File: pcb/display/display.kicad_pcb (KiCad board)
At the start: 2 copper layers, 15 x 44.2 mm, 7 parts, among them J1 INPUT, J2 OUTPUT, J3 UP, J4 DOWN, U1 74HC595

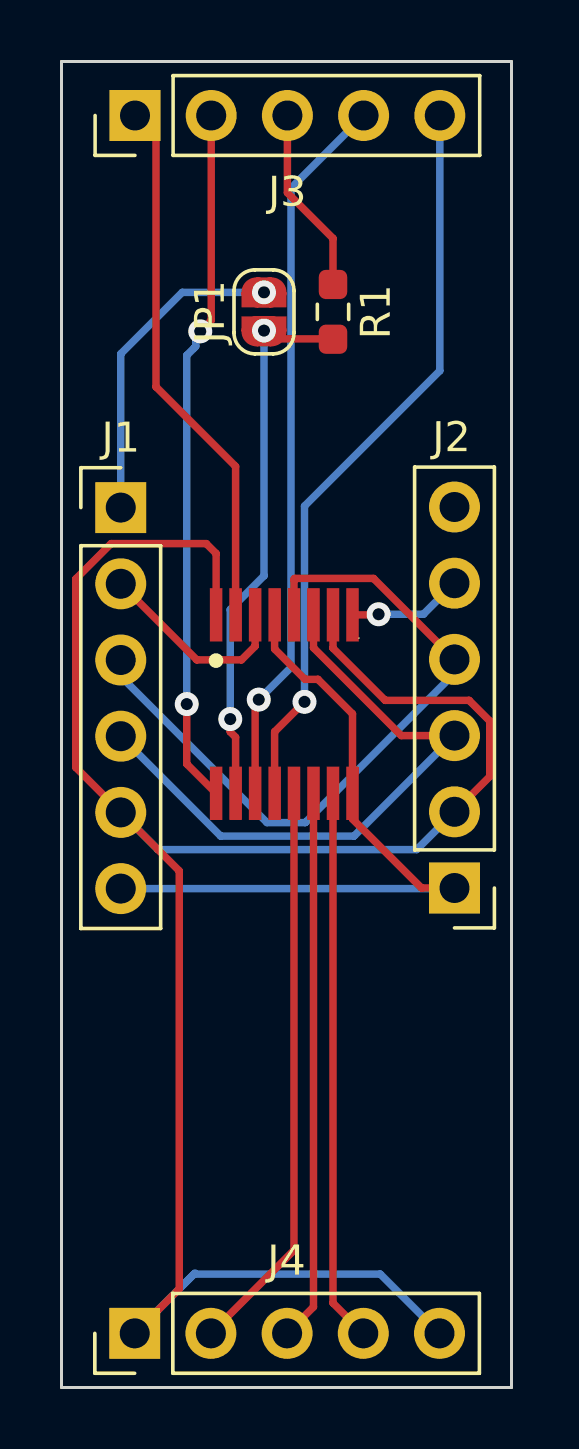
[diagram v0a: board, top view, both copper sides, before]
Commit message: chore: better silkscreen naming on display pcb
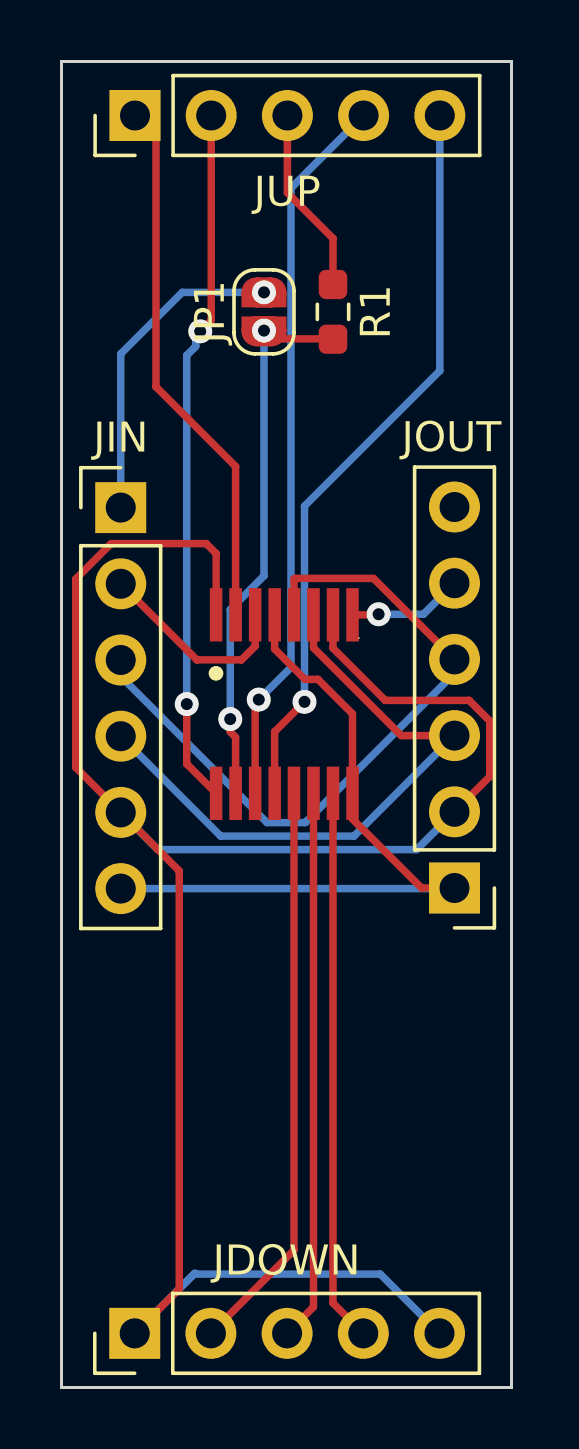
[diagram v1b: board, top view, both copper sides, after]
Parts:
- renumbered J4 to JDOWN, J1 to JIN, J2 to JOUT, J3 to JUP
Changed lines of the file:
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@@
 		(descr "Through hole straight pin header, 1x06, 2.54mm pitch, single row")
 		(tags "Through hole pin header THT 1x06 2.54mm single row")
-		(property "Reference" "J2"
+		(property "Reference" "JOUT"
 			(at 0.1 15.025 180)
 			(layer "F.SilkS")
@@
 		(descr "Through hole straight pin header, 1x05, 2.54mm pitch, single row")
 		(tags "Through hole pin header THT 1x05 2.54mm single row")
-		(property "Reference" "J4"
+		(property "Reference" "JDOWN"
 			(at 2.425 5.06 0)
 			(layer "F.SilkS")
@@
 		(descr "Through hole straight pin header, 1x06, 2.54mm pitch, single row")
 		(tags "Through hole pin header THT 1x06 2.54mm single row")
-		(property "Reference" "J1"
+		(property "Reference" "JIN"
 			(at 0 -2.33 0)
 			(layer "F.SilkS")
@@
 		(tags "solder jumper open")
 		(property "Reference" "JP1"
-			(at 0 -1.8 270)
+			(at 0 -1.8 -90)
 			(layer "F.SilkS")
 			(effects
@@
 		)
 		(property "Value" "SolderJumper_2_Open"
-			(at 0 1.9 270)
+			(at 0 1.9 -90)
 			(layer "F.Fab")
 			(hide yes)
@@
 		(descr "Through hole straight pin header, 1x05, 2.54mm pitch, single row")
 		(tags "Through hole pin header THT 1x05 2.54mm single row")
-		(property "Reference" "J3"
+		(property "Reference" "JUP"
 			(at -2.545 5.075 0)
 			(layer "F.SilkS")
@@
 	)
 	(gr_circle
-		(center 146.3 87.425)
-		(end 146.495256 87.425)
+		(center 146.3 87.85)
+		(end 146.495256 87.85)
 		(stroke
 			(width 0.1)

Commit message: feat(pcb): bus bars and led holder
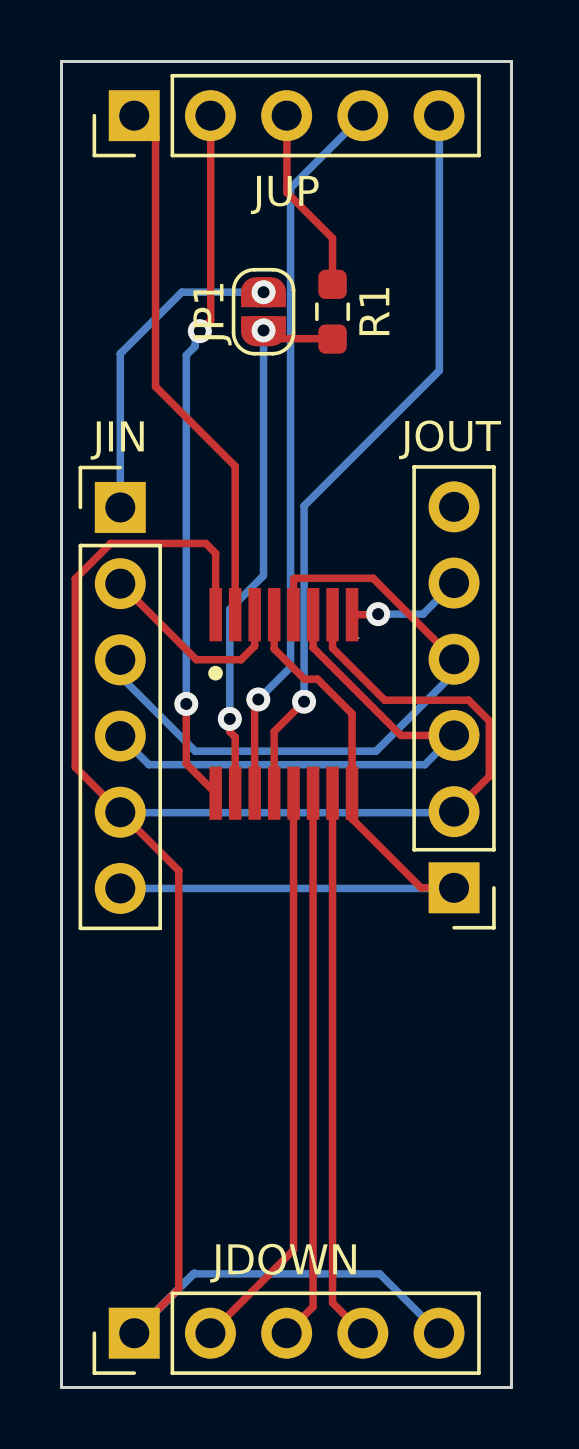
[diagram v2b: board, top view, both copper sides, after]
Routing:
- net STCP: track 23.9 -> 21.9 mm
- net SHCP: track 20.9 -> 18.9 mm
- net +5V: track 72.2 -> 71.2 mm
